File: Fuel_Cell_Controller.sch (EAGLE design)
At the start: 101 parts, among them J1 BLUETOOTH, U1 MAX232PTH

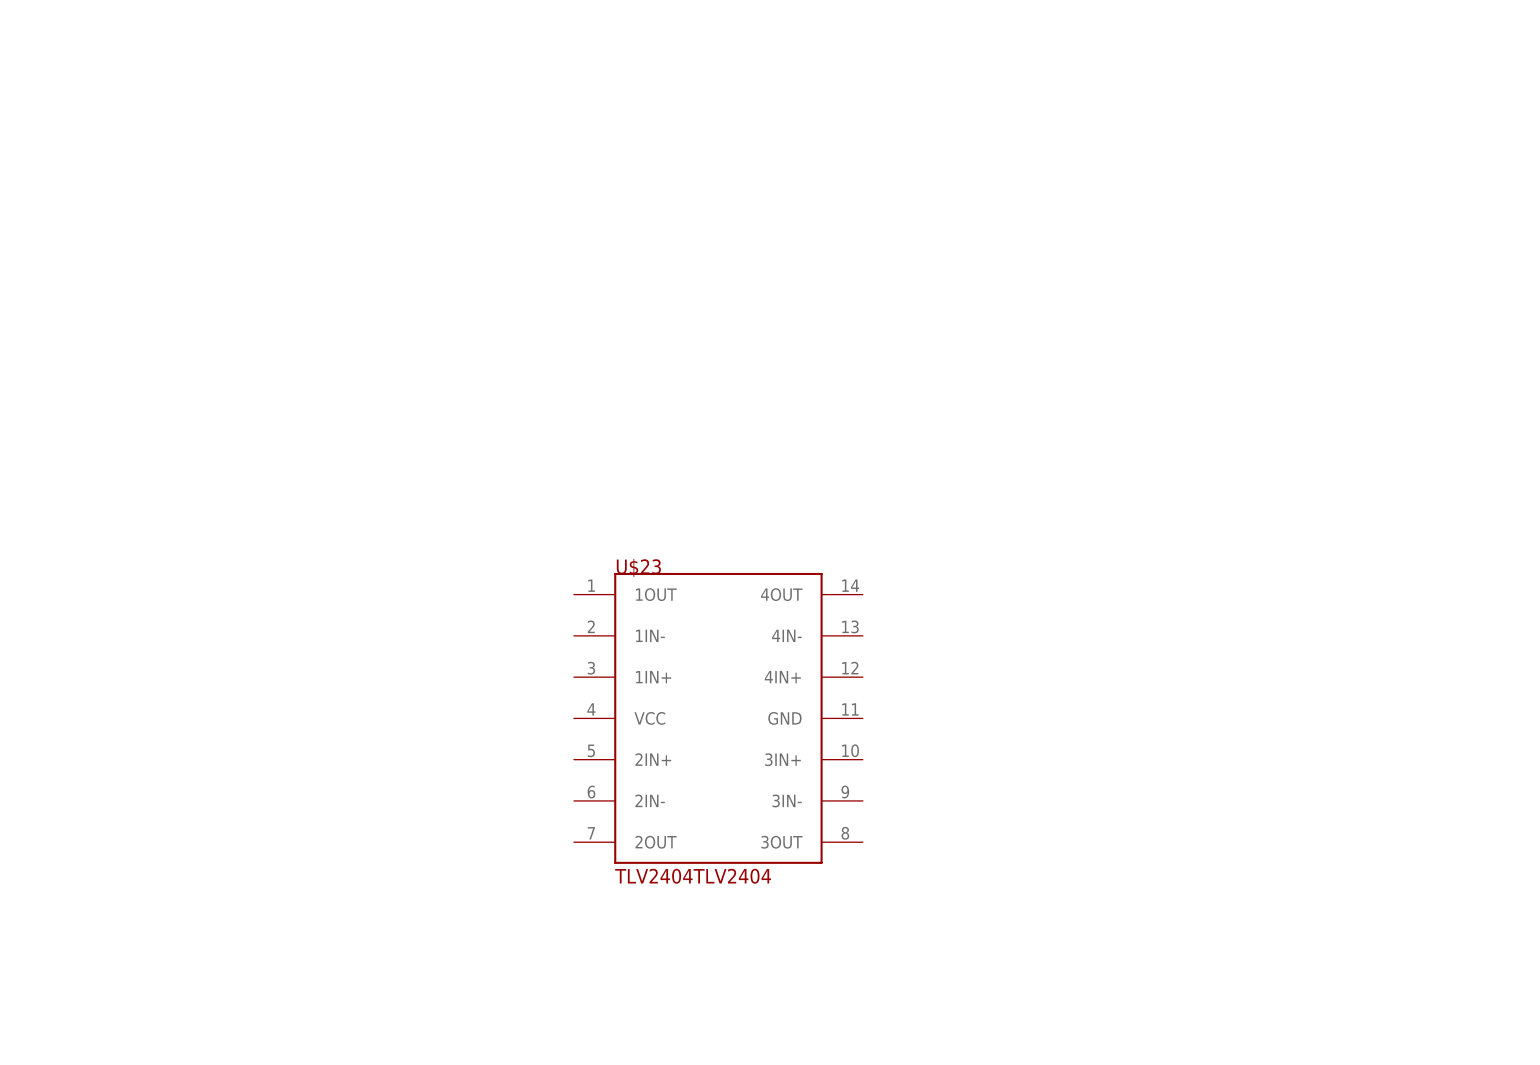
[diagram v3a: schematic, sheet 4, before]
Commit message: Implemented op amp for low-pass filter
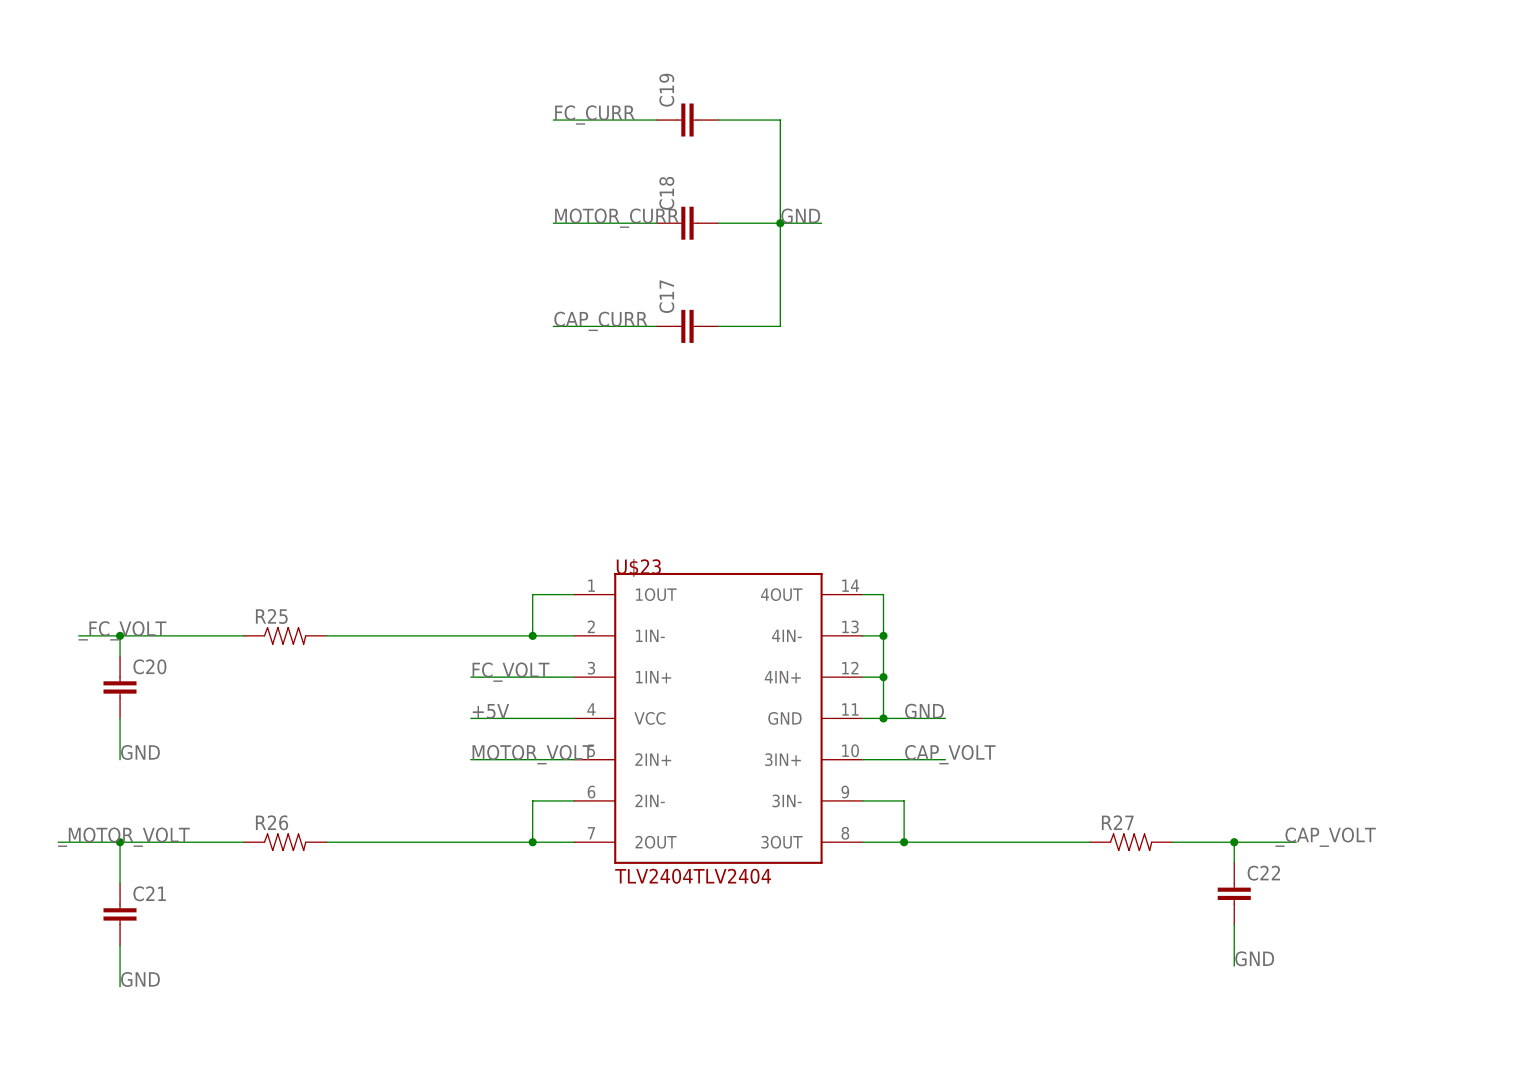
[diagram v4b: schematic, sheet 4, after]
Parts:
- added C17, C18, C19, C20, C21, C22: (no value), SparkFun-Capacitors:CAP0805
- added R25, R26, R27: (no value), SparkFun-Resistors:RESISTOR0805-RES
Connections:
- new net N$24: R25.2, U$23.1IN-, U$23.1OUT
- new net N$26: R26.2, U$23.2IN-, U$23.2OUT
- new net N$27: R27.1, U$23.3IN-, U$23.3OUT
- new net _CAP_VOLT: C22.1, R27.2, U$1.PA_4(ANALOGOUT/ANALOGIN/SPI1_SSEL)
- new net _FC_VOLT: C20.1, R25.1, U$1.PA_0(SERIAL4_TX/ANALOGIN/SERIAL2_CTS/PWM2/1)
- new net _MOTOR_VOLT: C21.1, R26.1, U$1.PA_3(A0/ANALOGIN/SERIAL2_RX/PWM2/4)
- net +5V: now also U$23.VCC
- net CAP_CURR: now also C17.1
- net CAP_VOLT: now also U$23.3IN+; no longer U$1.PA_4(ANALOGOUT/ANALOGIN/SPI1_SSEL)
- net FC_CURR: now also C19.1
- net FC_VOLT: now also U$23.1IN+; no longer U$1.PA_0(SERIAL4_TX/ANALOGIN/SERIAL2_CTS/PWM2/1)
- net GND: now also C17.2, C18.2, C19.2, C20.2, C21.2, C22.2, U$23.4IN+, U$23.4IN-, U$23.4OUT, U$23.GND
- net MOTOR_CURR: now also C18.1
- net MOTOR_VOLT: now also U$23.2IN+; no longer U$1.PA_3(A0/ANALOGIN/SERIAL2_RX/PWM2/4)

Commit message: Added starter relay and did more board layout
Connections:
- new net START_RELAY: ETH2.5, U$5.B5
- new net _START_RELAY: U$1.PC_7(SERIAL6_RX/PWM8/2), U$5.A5
- net CHARGE_RELAY: now also ETH2.6; no longer ETH2.5
- net GND: no longer ETH2.6, U$3.A6, U$3.A7, U$3.A8, U$3.B6, U$3.B7, U$3.B8, U$5.A8, U$5.B8
- net PWM_1: now also U$3.B6; no longer U$5.B5
- net PWM_2: now also U$3.B7; no longer U$5.B6
- net PWM_3: now also U$3.B8; no longer U$5.B7
- net _PWM_1: now also U$3.A6; no longer U$5.A5
- net _PWM_2: now also U$3.A7; no longer U$5.A6
- net _PWM_3: now also U$3.A8; no longer U$5.A7

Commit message: Added display, fixed power supplies
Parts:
- added C23: 1µF, SparkFun-Capacitors:CAP0805
- added U$30: ADAFRUITOLED, FCC_parts:ADAFRUITOLED
- added U$31: 641-1198-1-ND, 5V TVS:641-1198-1-ND
- added U$32: 1µF, 100uF_Cap:CAP-VS-SERIES-PACKAGE-E(ELECT)VS-SERIES-PACKAGE-E
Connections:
- removed net +5V: C14.1, C15.1, C3.1, C4.2, C8.1, J1.VCC, R1.1, R14.2, R15.2, R2.1, U$1.5V, U$2.RAW, U$21.C, U$23.VCC, U$28.+, U$3.VCC, U$5.VCC, U1.VCC
- removed net 3V3: C16.1, C6.1, C7.1, JP1.3, JP2.6, R16.1, SHTSENSOR.VIN, U$1.3V3, U$18.3.3V, U$19.VDD, U$20.VDD, U$24.DRAIN, U$26.P$1, U$27.+
- new net AUX3V3: SHTSENSOR.VIN, U$30.3.3VO
- new net GND1: C23.2, U$32.-
- new net NUC_3V3: C16.1, C6.1, C7.1, JP1.3, JP2.6, R16.1, U$1.3V3, U$18.3.3V, U$19.VDD, U$20.VDD, U$24.DRAIN, U$26.P$1, U$27.+
- new net OLED_CLK: U$1.PE_2(SPI4_SCLK), U$30.CLK
- new net OLED_MISO: U$1.PE_5(PWM9/1/SPI4_MISO), U$30.DC
- new net OLED_MOSI: U$1.PE_6(PWM9/2/SPI4_MOSI), U$30.DATA
- new net OLED_SEL: U$1.PE_4(SPI4_SSEL), U$30.CS
- net AUX5V: now also C23.1, J1.VCC, U$2.RAW, U$30.VIN, U$31.C, U$32.+
- net FC5V: now also C14.1, C15.1, C3.1, C4.2, C8.1, R1.1, R14.2, R15.2, R2.1, U$1.5V, U$21.C, U$23.VCC, U$28.+, U$3.VCC, U$5.VCC, U1.VCC
- net GND: now also U$30.GND, U$31.A
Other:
- note added: "OLED Display"
- moved on the sheet: U$21

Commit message: Started routing
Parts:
- added FC5-AUX5: (no value), SparkFun-Connectors:CONN_02
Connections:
- removed net GND1: C23.2, U$32.-
- removed net HUMID_RESET: U$1.PC_6(SERIAL6_TX/PWM8/1)
- removed net N$97: ETH1.6
- net AUX5V: now also FC5-AUX5.2
- net FC5V: now also FC5-AUX5.1
- net GND: now also C23.2, U$32.-
- net HUMID_RST: now also U$1.PC_6(SERIAL6_TX/PWM8/1)
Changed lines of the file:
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@@
 <part name="U$1" library="FCC_parts" deviceset="NUCLEO-F746ZG" device="NUCLEO-F746ZG"/>
 <part name="U$2" library="openlog" deviceset="OPENLOG" device=""/>
-<part name="GND1" library="E-P-008-R1.2" deviceset="GND" device=""/>
+<part name="GND" library="E-P-008-R1.2" deviceset="GND" device=""/>
 <part name="ETH7" library="ETHERNET" deviceset="ETHERNET" device=""/>
 <part name="ETH5" library="ETHERNET" deviceset="ETHERNET" device=""/>
@@
 <part name="C23" library="SparkFun-Capacitors" deviceset="CAP" device="0805" value="1µF"/>
 <part name="U$32" library="100uF_Cap" deviceset="CAP-VS-SERIES-PACKAGE-E(ELECT)" device="VS-SERIES-PACKAGE-E" value="1µF"/>
+<part name="FC5-AUX5" library="SparkFun-Connectors" library_urn="urn:adsk.eagle:library:513" deviceset="CONN_02" device="" package3d_urn="urn:adsk.eagle:package:38039/1"/>
 </parts>
 <sheets>
@@
 <wire x1="256.54" y1="-259.08" x2="256.54" y2="-215.9" width="0.1524" layer="94"/>
 <wire x1="482.6" y1="-45.72" x2="482.6" y2="0" width="0.1524" layer="94"/>
-<wire x1="497.84" y1="15.24" x2="474.98" y2="15.24" width="0.1524" layer="94"/>
 </plain>
 <instances>
 <instance part="U$1" gate="G$1" x="17.78" y="-5.08"/>
 <instance part="U$2" gate="G$1" x="157.48" y="48.26" rot="MR0"/>
-<instance part="GND1" gate="1" x="172.72" y="27.94"/>
+<instance part="GND" gate="1" x="172.72" y="27.94"/>
 <instance part="J1" gate="G$1" x="162.56" y="-2.54"/>
 <instance part="U1" gate="G$1" x="160.02" y="-58.42"/>
@@
 <wire x1="162.56" y1="35.56" x2="172.72" y2="35.56" width="0.1524" layer="91"/>
 <junction x="172.72" y="35.56"/>
-<pinref part="GND1" gate="1" pin="GND"/>
+<pinref part="GND" gate="1" pin="GND"/>
 </segment>
 <segment>
@@
 <wire x1="474.98" y1="15.24" x2="467.36" y2="15.24" width="0.1524" layer="91"/>
 <junction x="467.36" y="15.24"/>
+<pinref part="C23" gate="G$1" pin="2"/>
+<wire x1="490.22" y1="30.48" x2="490.22" y2="15.24" width="0.1524" layer="91"/>
+<pinref part="U$32" gate="G$1" pin="-"/>
+<wire x1="497.84" y1="30.48" x2="497.84" y2="15.24" width="0.1524" layer="91"/>
+<wire x1="490.22" y1="15.24" x2="474.98" y2="15.24" width="0.1524" layer="91"/>
+<wire x1="497.84" y1="15.24" x2="490.22" y2="15.24" width="0.1524" layer="91"/>
+<junction x="490.22" y="15.24"/>
+<junction x="474.98" y="15.24"/>
 </segment>
 <segment>
@@
 <label x="223.52" y="-68.58" size="1.778" layer="95"/>
 </segment>
+<segment>
+<pinref part="U$1" gate="G$1" pin="PC_6(SERIAL6_TX/PWM8/1)"/>
+<wire x1="-53.34" y1="-43.18" x2="-81.28" y2="-43.18" width="0.1524" layer="91"/>
+<label x="-81.28" y="-43.18" size="1.778" layer="95"/>
+</segment>
 </net>
 <net name="I2C1_SCL" class="0">
@@
 </segment>
 </net>
-<net name="HUMID_RESET" class="0">
-<segment>
-<pinref part="U$1" gate="G$1" pin="PC_6(SERIAL6_TX/PWM8/1)"/>
-<wire x1="-53.34" y1="-43.18" x2="-81.28" y2="-43.18" width="0.1524" layer="91"/>
-<label x="-81.28" y="-43.18" size="1.778" layer="95"/>
-</segment>
-</net>
 <net name="N$11" class="0">
 <segment>
@@
 </segment>
 </net>
-<net name="GND1" class="0">
-<segment>
-<pinref part="C23" gate="G$1" pin="2"/>
-<wire x1="490.22" y1="30.48" x2="490.22" y2="15.24" width="0.1524" layer="91"/>
-<pinref part="U$32" gate="G$1" pin="-"/>
-<wire x1="497.84" y1="30.48" x2="497.84" y2="15.24" width="0.1524" layer="91"/>
-</segment>
-</net>
 </nets>
 </sheet>
@@
 <wire x1="86.36" y1="213.36" x2="-15.24" y2="213.36" width="0.1524" layer="94"/>
 <wire x1="99.06" y1="213.36" x2="223.52" y2="213.36" width="0.1524" layer="94"/>
-<wire x1="223.52" y1="213.36" x2="223.52" y2="134.62" width="0.1524" layer="94"/>
-<wire x1="223.52" y1="134.62" x2="99.06" y2="134.62" width="0.1524" layer="94"/>
-<wire x1="99.06" y1="134.62" x2="99.06" y2="213.36" width="0.1524" layer="94"/>
+<wire x1="223.52" y1="213.36" x2="223.52" y2="121.92" width="0.1524" layer="94"/>
+<wire x1="223.52" y1="121.92" x2="99.06" y2="121.92" width="0.1524" layer="94"/>
+<wire x1="99.06" y1="121.92" x2="99.06" y2="213.36" width="0.1524" layer="94"/>
 </plain>
 <instances>
@@
 <instance part="ETH1" gate="G$1" x="20.32" y="182.88"/>
 <instance part="ETH9" gate="G$1" x="20.32" y="-154.94"/>
+<instance part="FC5-AUX5" gate="G$1" x="147.32" y="127"/>
 </instances>
 <busses>
@@
 <net name="AUX5V" class="0">
 <segment>
-<pinref part="AUX_PWR" gate="G$1" pin="5"/>
-<wire x1="198.12" y1="167.64" x2="170.18" y2="167.64" width="0.1524" layer="91"/>
-<wire x1="170.18" y1="167.64" x2="170.18" y2="198.12" width="0.1524" layer="91"/>
-<label x="170.18" y="198.12" size="1.778" layer="95" rot="R90"/>
+<wire x1="154.94" y1="129.54" x2="182.88" y2="129.54" width="0.1524" layer="91"/>
+<label x="167.64" y="129.54" size="1.778" layer="95"/>
+<pinref part="FC5-AUX5" gate="G$1" pin="2"/>
 </segment>
 <segment>
@@
 <label x="185.42" y="198.12" size="1.778" layer="95" rot="R90"/>
 </segment>
+<segment>
+<pinref part="AUX_PWR" gate="G$1" pin="5"/>
+<wire x1="198.12" y1="167.64" x2="170.18" y2="167.64" width="0.1524" layer="91"/>
+<wire x1="170.18" y1="167.64" x2="170.18" y2="198.12" width="0.1524" layer="91"/>
+<label x="170.18" y="198.12" size="1.778" layer="95" rot="R90"/>
+</segment>
 </net>
 <net name="GND" class="0">
@@
 <label x="43.18" y="127" size="1.778" layer="95"/>
 </segment>
+<segment>
+<wire x1="154.94" y1="127" x2="182.88" y2="127" width="0.1524" layer="91"/>
+<label x="167.64" y="127" size="1.778" layer="95"/>
+<pinref part="FC5-AUX5" gate="G$1" pin="1"/>
+</segment>
 </net>
 <net name="FAN1_PWR" class="0">
@@
 </segment>
 </net>
-<net name="N$97" class="0">
-<segment>
-<pinref part="ETH1" gate="G$1" pin="6"/>
-<wire x1="15.24" y1="185.42" x2="7.62" y2="185.42" width="0.1524" layer="91"/>
-</segment>
-</net>
 <net name="TEMP_4" class="0">
 <segment>
@@
 </sheet>
 </sheets>
+<errors>
+</errors>
 </schematic>
 </drawing>

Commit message: Continued routing
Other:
- note added: "Current Sensors LP Filter"
- note added: "Voltages LP Filter"
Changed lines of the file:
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@@
 <?xml version="1.0" encoding="utf-8"?>
 <!DOCTYPE eagle SYSTEM "eagle.dtd">
-<eagle version="8.4.1">
+<eagle version="8.4.0">
 <drawing>
 <settings>
@@
 <layer number="91" name="Nets" color="2" fill="1" visible="yes" active="yes"/>
 <layer number="92" name="Busses" color="1" fill="1" visible="yes" active="yes"/>
-<layer number="93" name="Pins" color="2" fill="1" visible="no" active="yes"/>
+<layer number="93" name="Pins" color="2" fill="1" visible="yes" active="yes"/>
 <layer number="94" name="Symbols" color="4" fill="1" visible="yes" active="yes"/>
 <layer number="95" name="Names" color="7" fill="1" visible="yes" active="yes"/>
@@
 <description>FC LP FILTER</description>
 <plain>
+<wire x1="-25.4" y1="86.36" x2="-25.4" y2="7.62" width="0.1524" layer="94"/>
+<wire x1="-25.4" y1="7.62" x2="160.02" y2="7.62" width="0.1524" layer="94"/>
+<wire x1="160.02" y1="7.62" x2="160.02" y2="86.36" width="0.1524" layer="94"/>
+<wire x1="160.02" y1="86.36" x2="83.82" y2="86.36" width="0.1524" layer="94"/>
+<wire x1="83.82" y1="86.36" x2="-5.08" y2="86.36" width="0.1524" layer="94"/>
+<wire x1="-5.08" y1="86.36" x2="-25.4" y2="86.36" width="0.1524" layer="94"/>
+<wire x1="-5.08" y1="86.36" x2="-5.08" y2="134.62" width="0.1524" layer="94"/>
+<wire x1="-5.08" y1="134.62" x2="83.82" y2="134.62" width="0.1524" layer="94"/>
+<wire x1="83.82" y1="134.62" x2="83.82" y2="86.36" width="0.1524" layer="94"/>
+<text x="0" y="129.54" size="1.778" layer="94">Current Sensors LP Filter</text>
+<text x="-17.78" y="78.74" size="1.778" layer="94">Voltages LP Filter</text>
 </plain>
 <instances>
@@
 <pinref part="C18" gate="G$1" pin="2"/>
 <wire x1="60.96" y1="109.22" x2="68.58" y2="109.22" width="0.1524" layer="91"/>
-<label x="68.58" y="109.22" size="1.778" layer="95"/>
+<label x="71.12" y="109.22" size="1.778" layer="95"/>
 <wire x1="68.58" y1="109.22" x2="73.66" y2="109.22" width="0.1524" layer="91"/>
 <wire x1="68.58" y1="96.52" x2="68.58" y2="109.22" width="0.1524" layer="91"/>
